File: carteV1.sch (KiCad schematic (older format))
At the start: 37 parts, among them J12 FILTER_IOUT_DUT2, J6 REF_CLK_DUT2, J7 CRYSTAL OUTDUT2, T4 BALUN, X1 25mhz

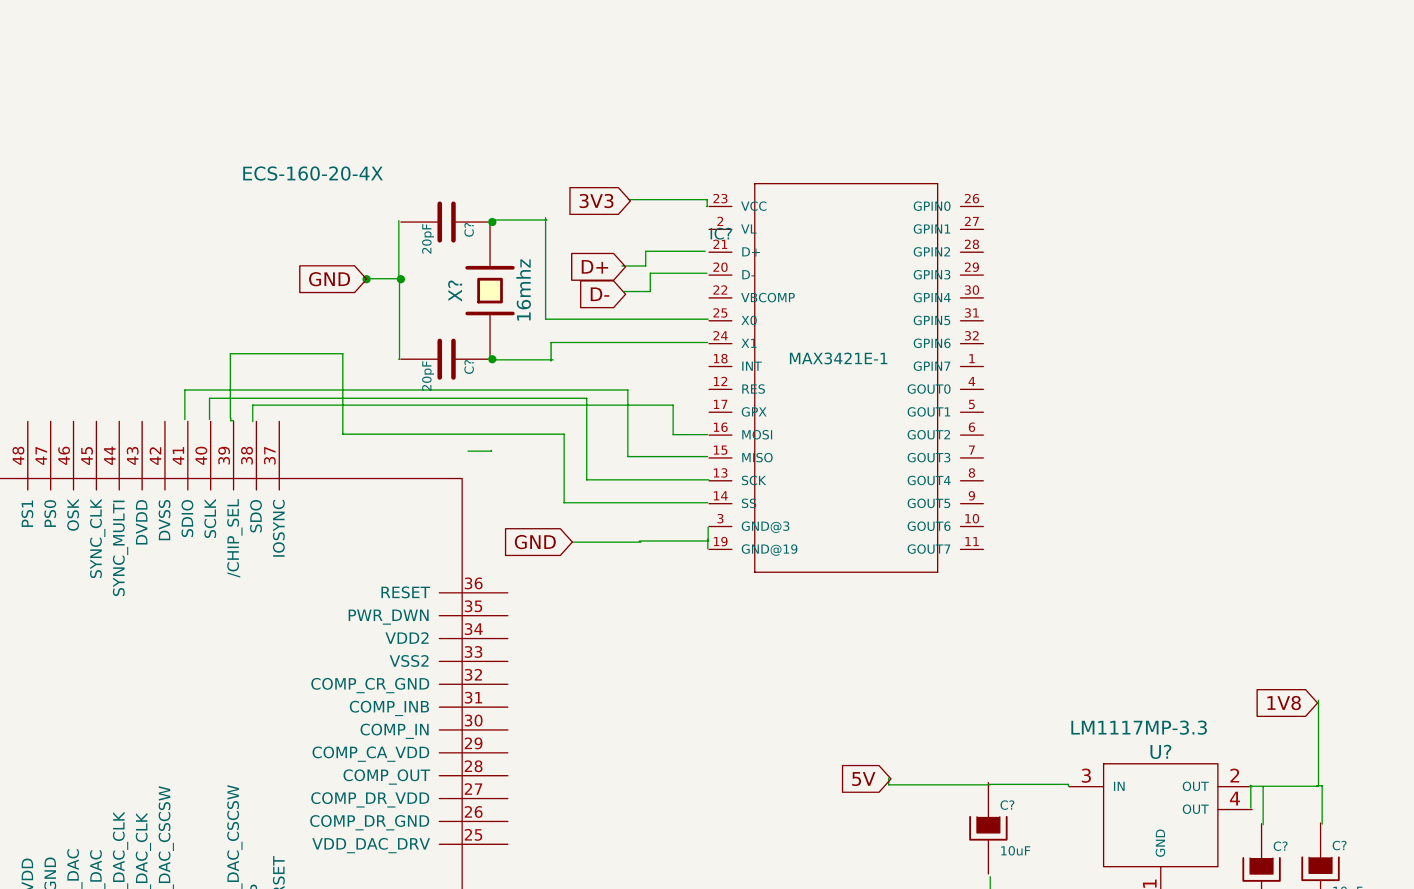
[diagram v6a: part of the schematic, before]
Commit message: USB changement PARTS
-Utilisation du MCP2210 ( SPI-MASTER)
-Changement du Quartz
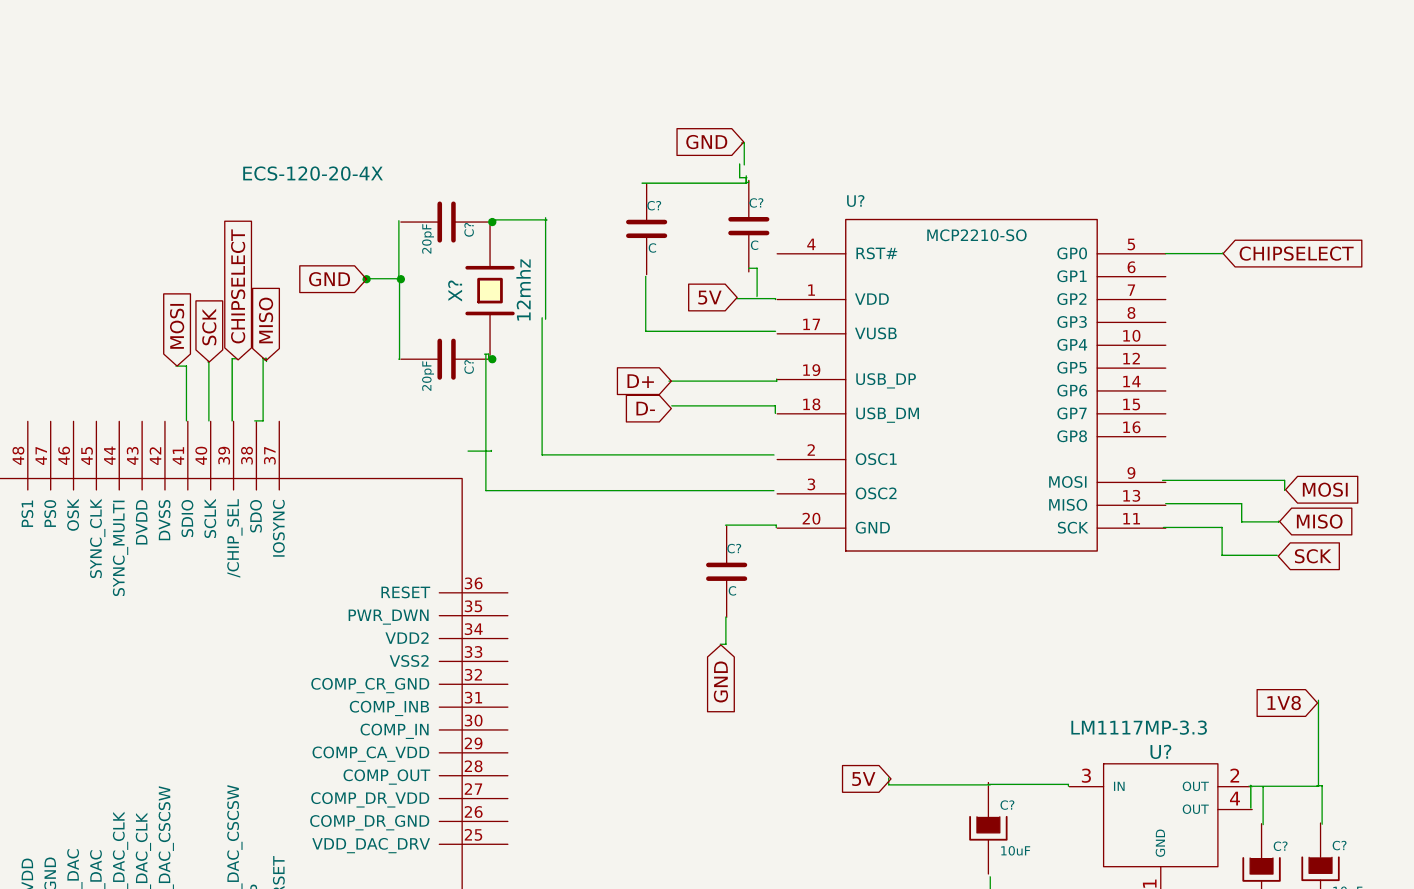
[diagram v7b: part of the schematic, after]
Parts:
- removed IC?: MAX3421E-1, TQFP32-5MM, symbol MAX3421E-1
- added C? (x3): C, ~, symbol C
- added U?: MCP2210-SO, SSOP-20, symbol MCP2210-SO
- X?: value 16mhz -> 12mhz
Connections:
- net labels added: CHIPSELECT, MISO, MOSI, SCK
- wire segments 169 -> 183
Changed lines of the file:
@@
 LIBS:Power_kl
 LIBS:FE
+LIBS:mcp2210
 LIBS:carteV1-cache
 EELAYER 27 0
@@
 Sheet 1 1
 Title "AD9954 - GENERATION SIGNAL HF"
-Date "19 may 2014"
+Date "20 may 2014"
 Rev "0.1"
 Comp "Polytech'Tours"
@@
 $EndComp
 $Comp
-L GND #PWR?
+L GND #PWR01
 U 1 1 53791D95
 P 4050 7600
-F 0 "#PWR?" H 4050 7600 30  0001 C CNN
+F 0 "#PWR01" H 4050 7600 30  0001 C CNN
 F 1 "GND" H 4050 7530 30  0001 C CNN
 F 2 "" H 4050 7600 60  0000 C CNN
@@
 $EndComp
 $Comp
-L MAX3421E-1 IC?
-U 1 1 537A7593
-P 8698 1532
-F 0 "IC?" H 8098 2082 50  0000 L BNN
-F 1 "MAX3421E-1" H 8445 1536 50  0000 L BNN
-F 2 "TQFP32-5MM" H 8698 1682 50  0001 C CNN
-F 3 "" H 8698 1532 60  0000 C CNN
-	1    8698 1532
-	1    0    0    -1
-$EndComp
-$Comp
 L LM1117MP-3.3 U?
 U 1 1 537A8393
@@
 	1    0    0    -1
 $EndComp
-Text GLabel 7754 808  0    60   Input ~ 0
-3V3
 $Comp
 L AD9954 U?
@@
 P 7140 1200
 F 0 "X?" H 7140 1350 60  0000 C CNN
-F 1 "16mhz" H 7140 1050 60  0000 C CNN
+F 1 "12mhz" H 7140 1050 60  0000 C CNN
 F 2 "~" H 7140 1200 60  0000 C CNN
-F 3 " ECS-160-20-4X" V 7650 1977 60  0000 C CNN
+F 3 " ECS-120-20-4X" V 7650 1977 60  0000 C CNN
 	1    7140 1200
 	0    -1   -1   0
@@
 	0    1    1    0
 $EndComp
-Text GLabel 7733 1096 0    60   Input ~ 0
+Text GLabel 7933 1596 0    60   Input ~ 0
 D+
-Text GLabel 7733 1216 0    60   Input ~ 0
+Text GLabel 7933 1716 0    60   Input ~ 0
 D-
 Text GLabel 9133 5796 0    60   Input ~ 0
@@
 Text GLabel 9500 6250 0    60   Input ~ 0
 GND
-Wire Wire Line
-	7563 2028 8097 2028
-Wire Wire Line
-	7563 1671 7563 2028
-Wire Wire Line
-	5913 1671 7563 1671
-Wire Wire Line
-	5913 1764 5913 1671
-Wire Wire Line
-	7743 1926 8091 1926
-Wire Wire Line
-	7743 1635 7743 1926
-Wire Wire Line
-	5805 1635 7743 1635
-Wire Wire Line
-	5805 1764 5805 1635
-Wire Wire Line
-	7941 1830 8091 1830
-Wire Wire Line
-	7941 1701 7941 1830
-Wire Wire Line
-	6102 1701 7941 1701
-Wire Wire Line
-	6102 1773 6102 1701
+$Comp
+L MCP2210-SO U?
+U 1 1 537ABAA0
+P 8696 889
+F 0 "U?" H 8696 939 50  0000 L BNN
+F 1 "MCP2210-SO" H 9046 789 50  0000 L BNN
+F 2 "SSOP-20" H 9046 739 50  0001 L CNN
+F 3 "~" H 9766 -1086 60  0000 C CNN
+	1    8696 889
+	1    0    0    -1
+$EndComp
+Text GLabel 10620 2071 2    60   Input ~ 0
+MOSI
+Text GLabel 10594 2210 2    60   Input ~ 0
+MISO
+Text GLabel 10588 2362 2    60   Input ~ 0
+SCK
+Text GLabel 5771 1530 1    60   Input ~ 0
+MOSI
+Text GLabel 6160 1506 1    60   Input ~ 0
+MISO
+Text GLabel 5912 1512 1    60   Input ~ 0
+SCK
+Text GLabel 8221 1230 0    60   Input ~ 0
+5V
+Text GLabel 8250 550  0    60   Input ~ 0
+GND
+$Comp
+L C C?
+U 1 1 537AD1AA
+P 8272 918
+F 0 "C?" H 8272 1018 40  0000 L CNN
+F 1 "C" H 8278 833 40  0000 L CNN
+F 2 "~" H 8310 768 30  0000 C CNN
+F 3 "~" H 8272 918 60  0000 C CNN
+	1    8272 918
+	1    0    0    -1
+$EndComp
+$Comp
+L C C?
+U 1 1 537AD513
+P 7825 930
+F 0 "C?" H 7825 1030 40  0000 L CNN
+F 1 "C" H 7831 845 40  0000 L CNN
+F 2 "~" H 7863 780 30  0000 C CNN
+F 3 "~" H 7825 930 60  0000 C CNN
+	1    7825 930
+	1    0    0    -1
+$EndComp
+$Comp
+L C C?
+U 1 1 537AD6CE
+P 8175 2430
+F 0 "C?" H 8175 2530 40  0000 L CNN
+F 1 "C" H 8181 2345 40  0000 L CNN
+F 2 "~" H 8213 2280 30  0000 C CNN
+F 3 "~" H 8175 2430 60  0000 C CNN
+	1    8175 2430
+	1    0    0    -1
+$EndComp
+Text GLabel 8150 2750 3    60   Input ~ 0
+GND
+Text GLabel 10347 1038 2    60   Input ~ 0
+CHIPSELECT
+Text GLabel 6038 1503 1    60   Input ~ 0
+CHIPSELECT
 Wire Wire Line
 	9806 6246 9806 6264
@@
 	9126 5792 9334 5792
 Wire Wire Line
-	7841 1124 8089 1124
-Wire Wire Line
-	7841 1204 7841 1124
-Wire Wire Line
-	7725 1204 7841 1204
-Wire Wire Line
-	7821 1028 8081 1028
-Wire Wire Line
-	7821 1092 7821 1028
-Wire Wire Line
-	7717 1092 7821 1092
-Wire Wire Line
 	6744 1500 6741 1500
 Wire Wire Line
@@
 	6741 894  6741 1143
 Wire Wire Line
-	7383 1325 8094 1325
-Wire Wire Line
 	7383 881  7383 1325
-Wire Wire Line
-	7407 1427 8091 1427
-Wire Wire Line
-	7407 1508 7407 1427
 Connection ~ 7150 900
 Connection ~ 7150 1500
 Wire Wire Line
 	7389 891  7137 891
-Wire Wire Line
-	7146 1503 7416 1503
 Wire Wire Line
 	7044 1902 7146 1902
@@
 	9328 3870 9328 3764
 Wire Wire Line
-	7745 802  8090 802
-Wire Wire Line
-	8090 802  8090 832
-Wire Wire Line
-	8090 832  8087 832
-Wire Wire Line
-	6004 1756 6004 1476
-Wire Wire Line
-	6004 1476 6496 1476
-Wire Wire Line
-	6496 1476 6496 1828
-Wire Wire Line
-	6496 1828 7464 1828
-Wire Wire Line
-	7464 1828 7464 2128
-Wire Wire Line
-	7464 2128 8092 2128
-Wire Wire Line
-	6006 1757 6006 1769
-Wire Wire Line
-	6006 1769 6018 1769
-Text GLabel 7500 2300 0    60   Input ~ 0
-GND
-Wire Wire Line
-	7500 2300 7800 2300
-Wire Wire Line
-	7794 2295 8094 2295
-Wire Wire Line
-	8094 2295 8094 2235
-Wire Wire Line
-	8093 2330 8093 2289
-Wire Wire Line
-	8093 2289 8091 2289
+	10082 2030 10616 2030
+Wire Wire Line
+	10616 2030 10616 2074
+Wire Wire Line
+	10096 2132 10428 2132
+Wire Wire Line
+	10428 2132 10428 2212
+Wire Wire Line
+	10428 2212 10590 2212
+Wire Wire Line
+	10590 2212 10590 2208
+Wire Wire Line
+	10086 2236 10342 2236
+Wire Wire Line
+	10342 2236 10342 2358
+Wire Wire Line
+	10342 2358 10584 2358
+Wire Wire Line
+	5910 1770 5910 1512
+Wire Wire Line
+	5910 1512 5906 1512
+Wire Wire Line
+	5812 1770 5812 1530
+Wire Wire Line
+	5812 1530 5766 1530
+Wire Wire Line
+	6162 1496 6156 1496
+Wire Wire Line
+	6111 1770 6147 1770
+Wire Wire Line
+	6147 1770 6147 1497
+Wire Wire Line
+	6147 1497 6150 1497
+Wire Wire Line
+	6153 1503 6162 1503
+Wire Wire Line
+	6162 1503 6162 1510
+Wire Wire Line
+	7368 1319 7368 1919
+Wire Wire Line
+	7368 1919 8382 1919
+Wire Wire Line
+	7122 1481 7122 2075
+Wire Wire Line
+	7122 2075 8382 2075
+Wire Wire Line
+	7134 1496 7134 1478
+Wire Wire Line
+	7134 1478 7116 1478
+Wire Wire Line
+	7923 1596 8394 1596
+Wire Wire Line
+	8394 1596 8394 1587
+Wire Wire Line
+	7935 1704 8388 1704
+Wire Wire Line
+	8388 1704 8388 1737
+Wire Wire Line
+	8219 1235 8389 1235
+Wire Wire Line
+	8389 1235 8389 1239
+Wire Wire Line
+	8252 554  8240 554
+Wire Wire Line
+	8252 650  8252 554
+Wire Wire Line
+	8272 1102 8308 1102
+Wire Wire Line
+	8308 1102 8308 1226
+Wire Wire Line
+	8232 646  8232 706
+Wire Wire Line
+	8232 706  8264 706
+Wire Wire Line
+	8261 710  8261 727
+Wire Wire Line
+	8261 727  8271 727
+Wire Wire Line
+	8271 727  8271 721
+Wire Wire Line
+	7821 1138 7821 1378
+Wire Wire Line
+	7821 1378 8389 1378
+Wire Wire Line
+	7805 730  8261 730
+Wire Wire Line
+	8261 730  8261 698
+Wire Wire Line
+	8170 2226 8392 2226
+Wire Wire Line
+	8392 2226 8392 2236
+Wire Wire Line
+	8172 2627 8172 2747
+Wire Wire Line
+	8172 2747 8147 2747
+Wire Wire Line
+	10095 1038 10345 1038
+Wire Wire Line
+	10345 1038 10345 1035
+Wire Wire Line
+	6012 1770 6012 1498
+Wire Wire Line
+	6012 1498 6032 1498
 $EndSCHEMATC

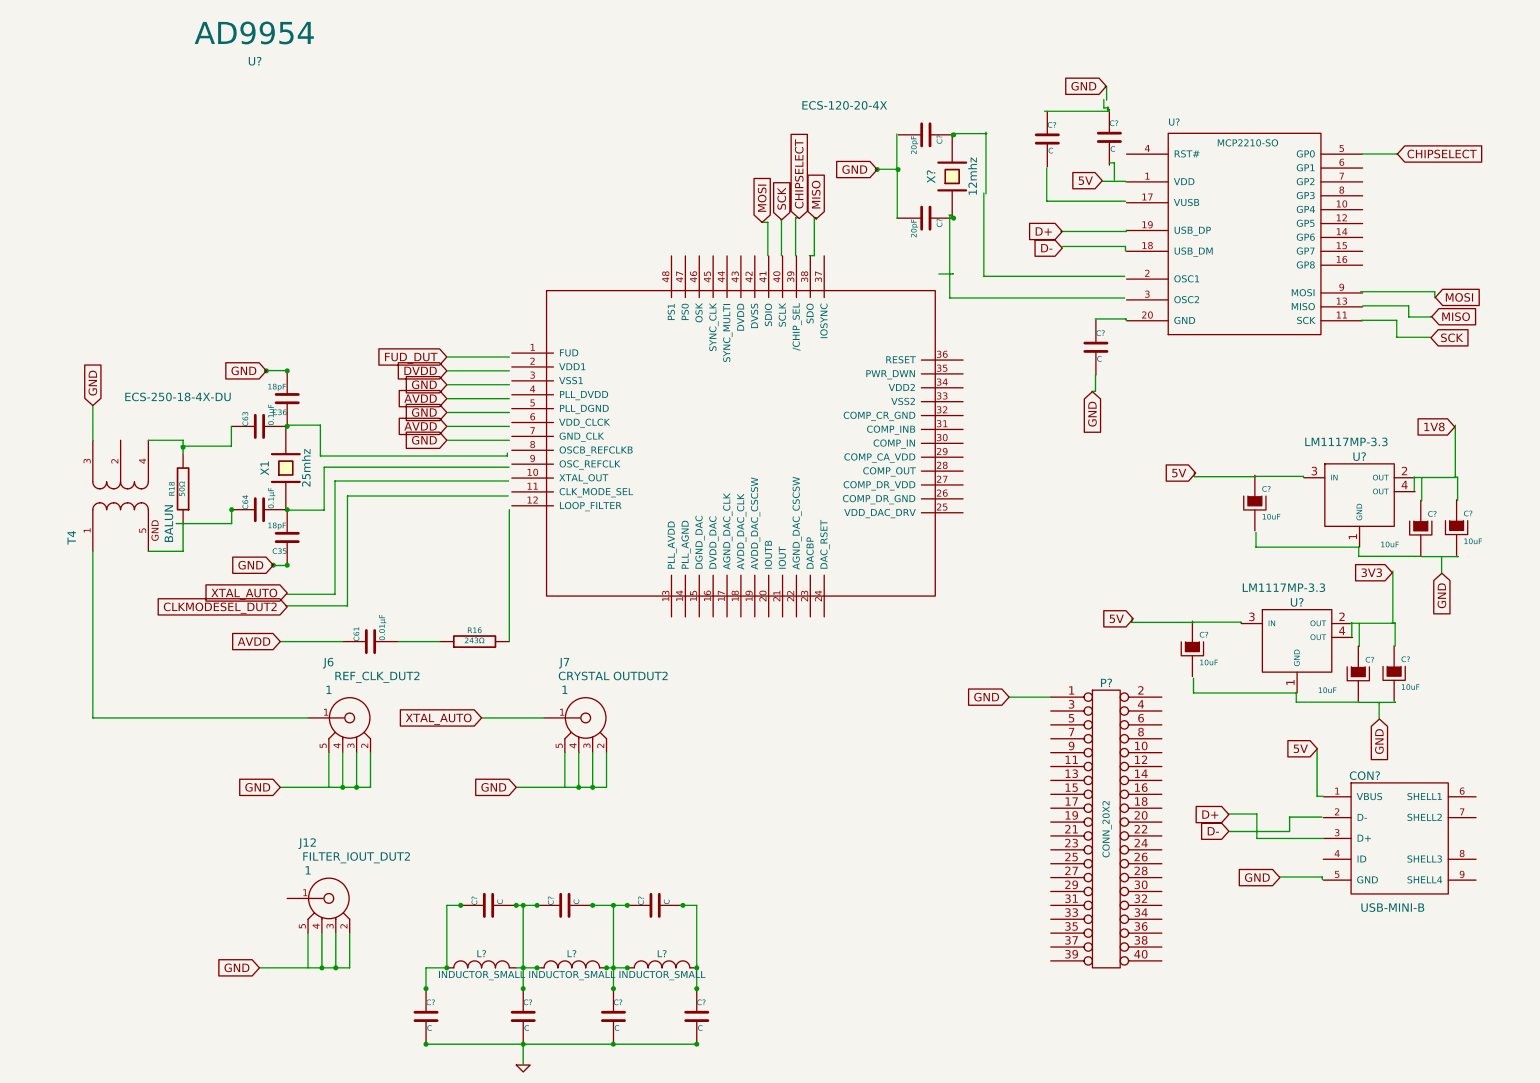
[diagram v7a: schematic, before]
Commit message: Alimentation
-Ajout des deux montages
-Fin du raccordement du microC
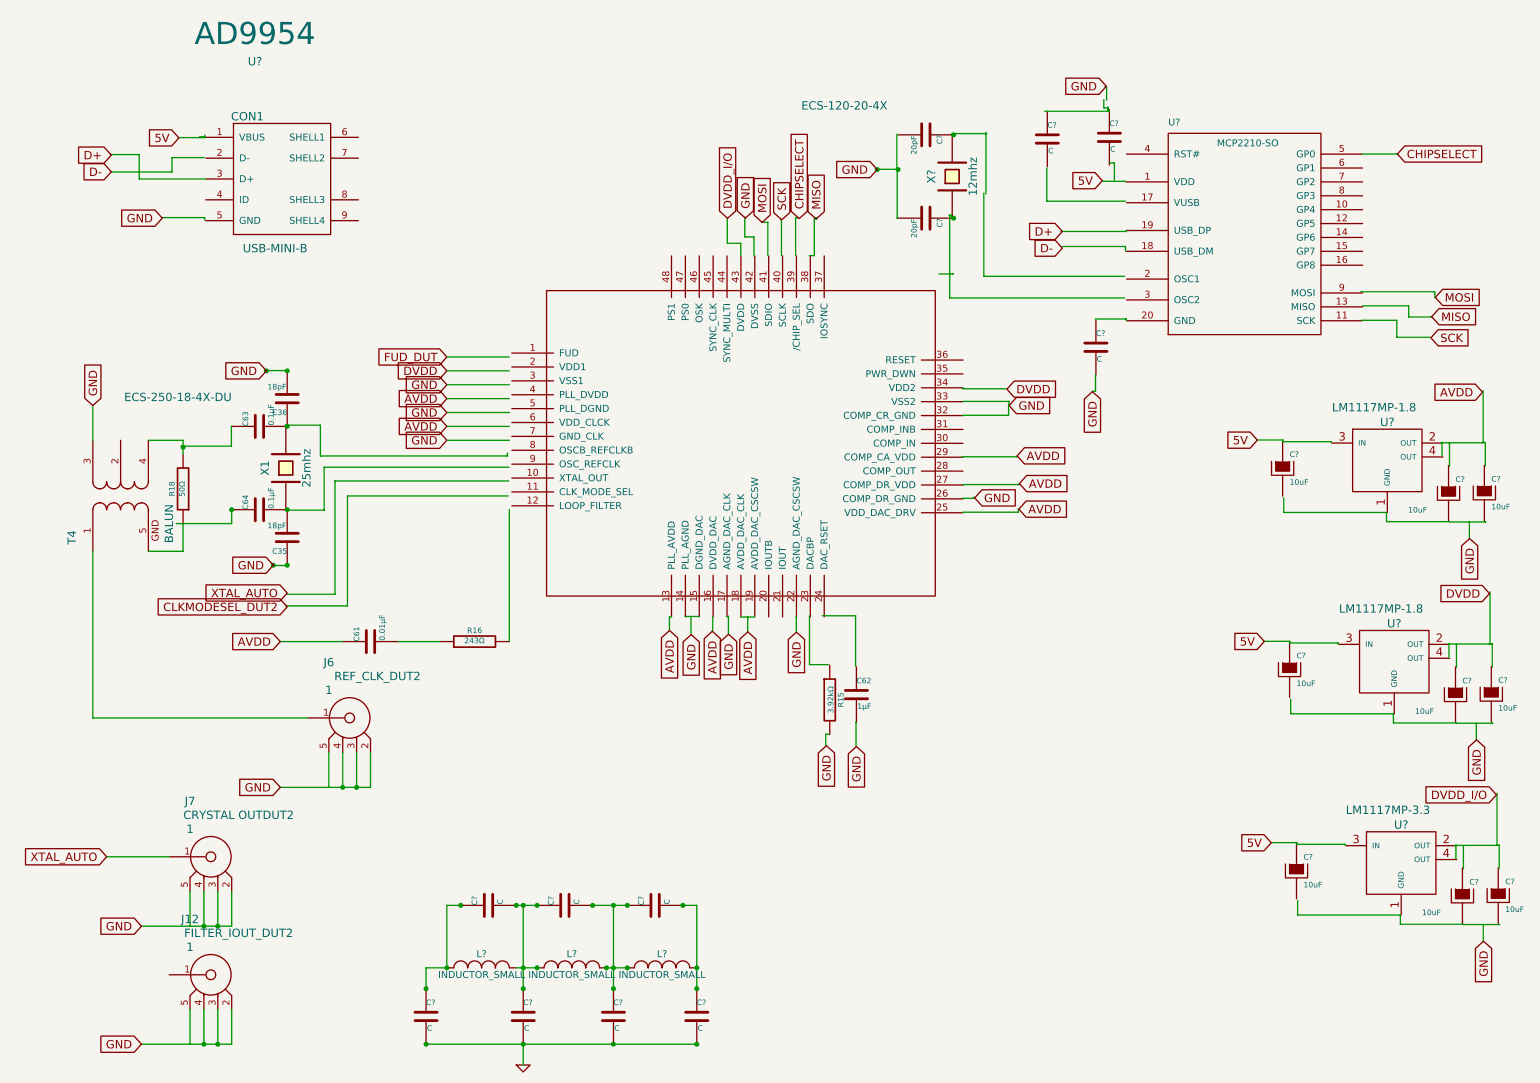
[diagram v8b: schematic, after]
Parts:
- removed C? (x3): 10uF, ~, symbol CAPAPOL
- removed P?: CONN_20X2, symbol CONN_20X2
- removed U?: LM1117MP-3.3, symbol LM1117MP-3.3
- added C62: 1μF, ~, symbol C
- added C? (x6): 10uF, ~, symbol CAPAPOL
- added R15: 3.92kΩ, ~, symbol R
- added U? (x2): LM1117MP-1.8, symbol LM1117MP-3.3
- gave numbers to parts that had none: 1
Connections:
- net labels added: DVDD_I/O
- net labels removed: 1V8, 3V3
- wire segments 183 -> 243
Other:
- moved on the sheet: C?, CON1, J12, J7, U?
